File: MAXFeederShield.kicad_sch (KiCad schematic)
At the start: 40 parts, among them J1 Conn_01x04_Male, J10 Conn_01x04_Male, J11 Conn_01x04_Male, J12 Conn_01x04_Male, J13 Conn_01x04_Male, J14 Conn_01x04_Male, J15 Conn_01x04_Male, J16 Conn_01x04_Male, J17 Conn_01x04_Male, J18 Conn_01x04_Male, J19 Conn_01x04_Male, J2 Barrel_Jack_Switch, J20 Conn_01x04_Male, J22 Conn_01x04_Male, J23 Conn_01x04_Male, J24 Conn_01x04_Male, J25 Conn_01x04_Male, J26 Conn_01x04_Male, J27 Conn_01x04_Male, J28 Conn_01x04_Male, J29 Conn_01x04_Male, J3 Conn_01x04_Male, J30 Conn_01x04_Male, J31 Conn_01x04_Male, J32 Conn_01x04_Male, J33 Conn_01x04_Male, J34 Conn_01x04_Male, J35 Conn_01x04_Male, J36 Conn_01x04_Male, J37 Screw_Terminal_01x02, J4 Conn_01x04_Male, J5 Conn_01x04_Male, J6 Conn_01x04_Male, J7 Conn_01x04_Male, J8 Conn_01x04_Male, J9 Conn_01x04_Male, SW1 SW_Push_Dual

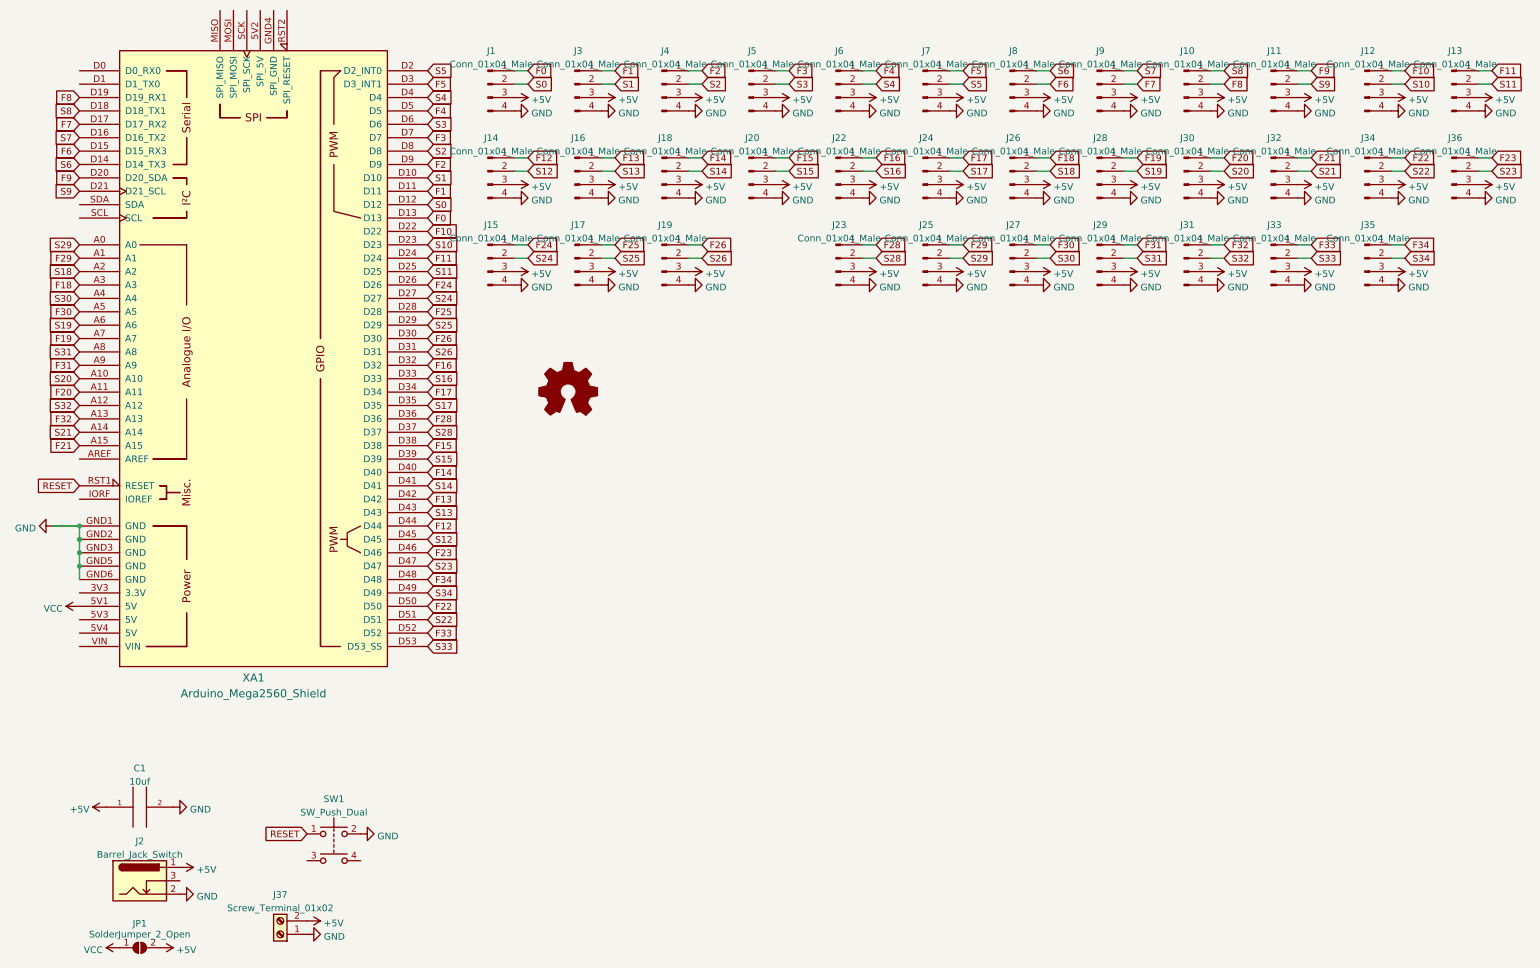
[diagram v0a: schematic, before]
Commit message: Redesigned shield PCB, as well as adapter PCB, modified 0816 feeder firmware
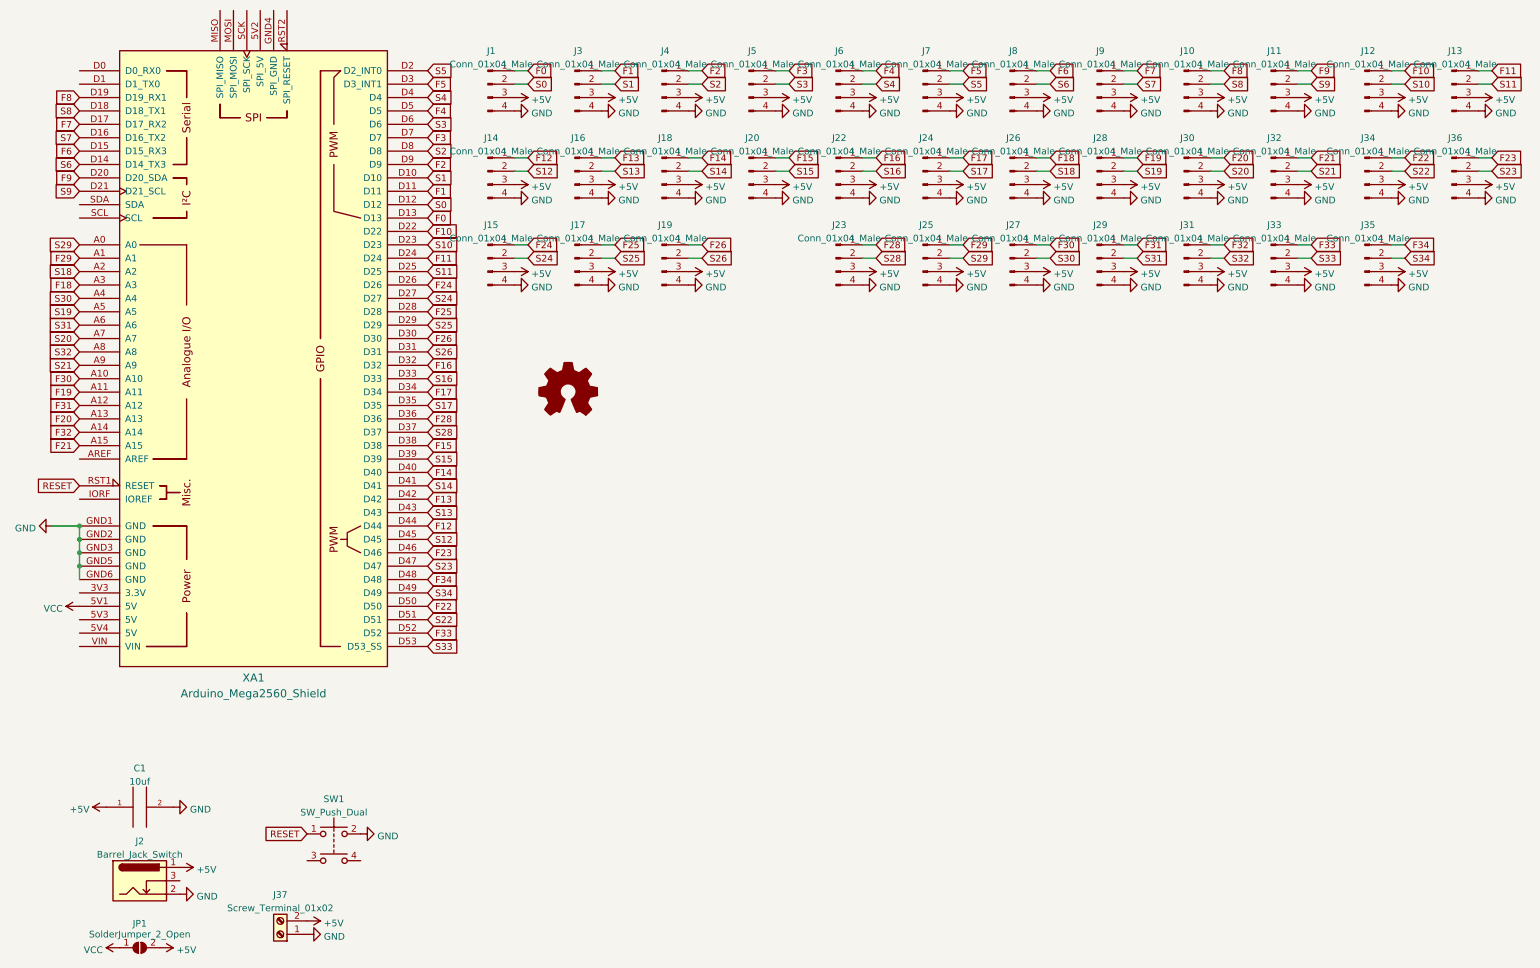
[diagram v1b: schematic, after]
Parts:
- J1, J10, J11, J12, J13, J14, J15, J16, J17, J18, J19, J20, J22, J23, J24, J25, J26, J27, J28, J29, J3, J30, J31, J32, J33, J34, J35, J36, J4, J5, J6, J7, J8, J9: footprint Connector_JST:JST_EH_B4B-EH-A_1x04_P2.50mm_Vertical -> JST:JST_EH_B4B-EH-A_1x04_P2.50mm_Vertical_LOCKING
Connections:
- net F19: now also XA1.A11; no longer XA1.A7
- net F20: now also XA1.A13; no longer XA1.A11
- net F30: now also XA1.A10; no longer XA1.A5
- net F31: now also XA1.A12; no longer XA1.A9
- net F32: now also XA1.A14; no longer XA1.A13
- net F6: now also J8.1 (Pin_1); no longer J8.2 (Pin_2)
- net F7: now also J9.1 (Pin_1); no longer J9.2 (Pin_2)
- net F8: now also J10.1 (Pin_1); no longer J10.2 (Pin_2)
- net S19: now also XA1.A5; no longer XA1.A6
- net S20: now also XA1.A7; no longer XA1.A10
- net S21: now also XA1.A9; no longer XA1.A14
- net S31: now also XA1.A6; no longer XA1.A8
- net S32: now also XA1.A8; no longer XA1.A12
- net S6: now also J8.2 (Pin_2); no longer J8.1 (Pin_1)
- net S7: now also J9.2 (Pin_2); no longer J9.1 (Pin_1)
- net S8: now also J10.2 (Pin_2); no longer J10.1 (Pin_1)
